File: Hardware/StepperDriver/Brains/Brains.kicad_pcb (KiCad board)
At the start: 2 copper layers, 79.6 x 72.6 mm, 18 parts, among them IC1 ATMEGA328-P, P1 CONN_01X02, P2 CONN_01X02, P3 CONN_01X07, P4 CONN_01X07, P5 CONN_01X07, P6 CONN_01X04, Y1 Crystal

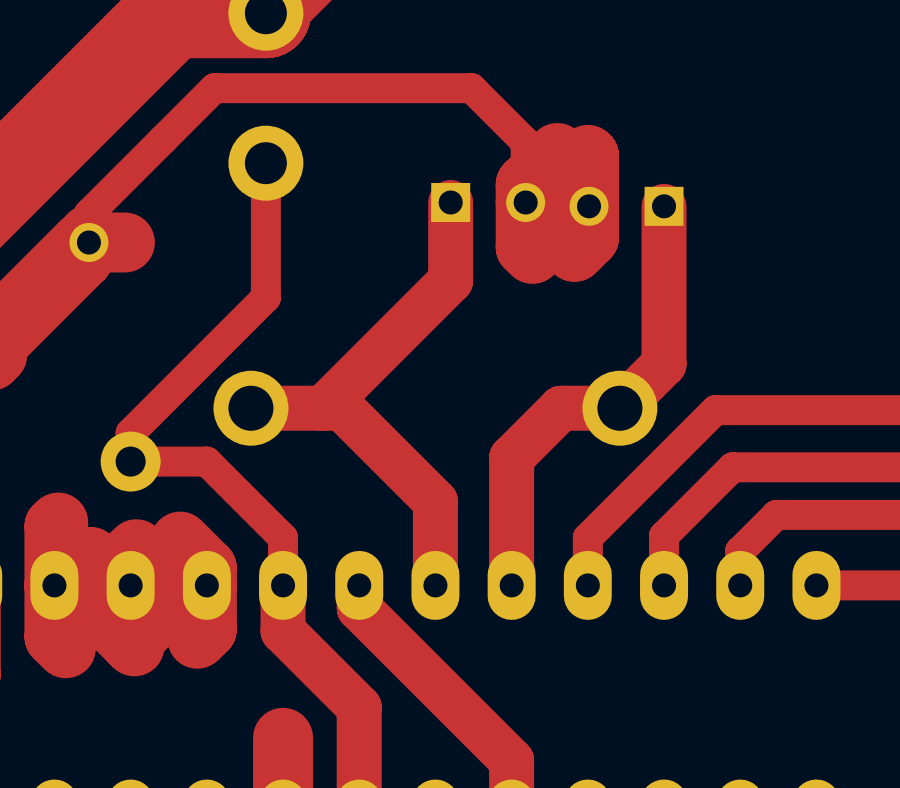
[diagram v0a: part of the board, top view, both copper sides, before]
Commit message: fixed incorrect Xtal footprint
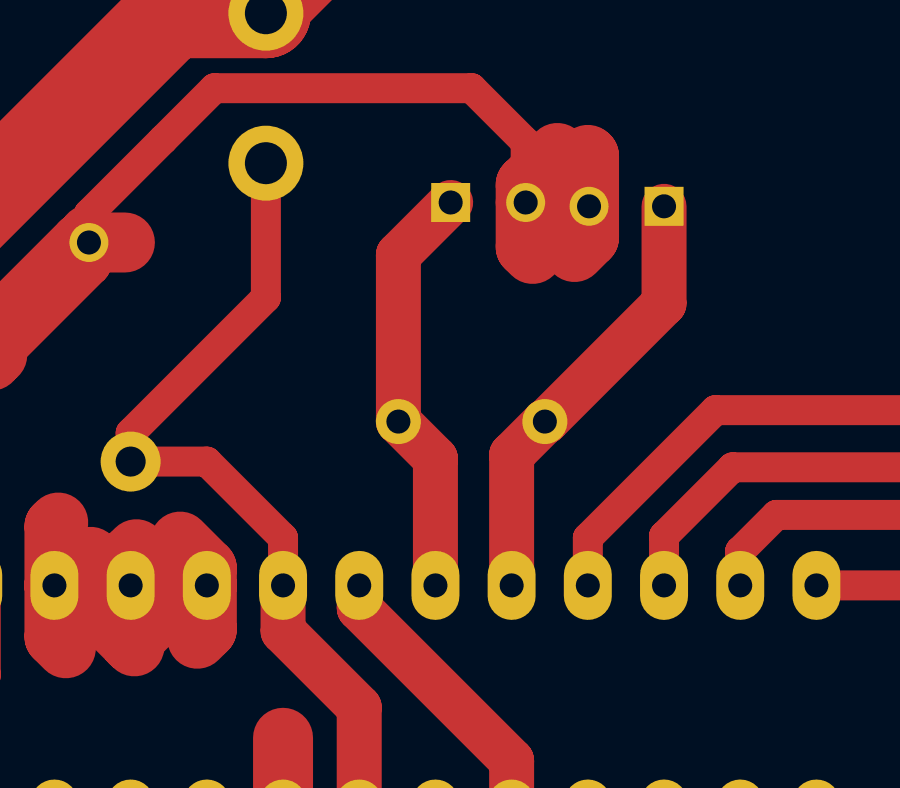
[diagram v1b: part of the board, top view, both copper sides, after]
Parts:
- Y1: footprint Crystals:Crystal_HC48-U_Vertical -> Crystals:Crystal_HC49-U_Vertical
- moved Y1 1.29 mm to (95.8, 48.1)
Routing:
- net Net-(C4-Pad1): track 18.9 -> 14.0 mm
- net Net-(C3-Pad1): track 15.9 -> 14.8 mm
